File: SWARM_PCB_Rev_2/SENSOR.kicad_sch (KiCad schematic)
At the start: 14 parts

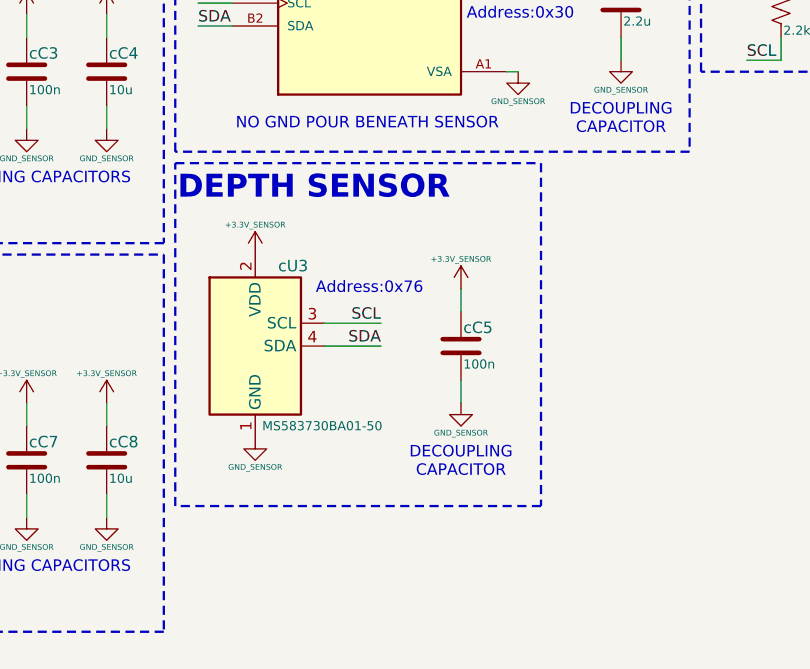
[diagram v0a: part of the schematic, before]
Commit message: Fixed some small errors and added the Output board
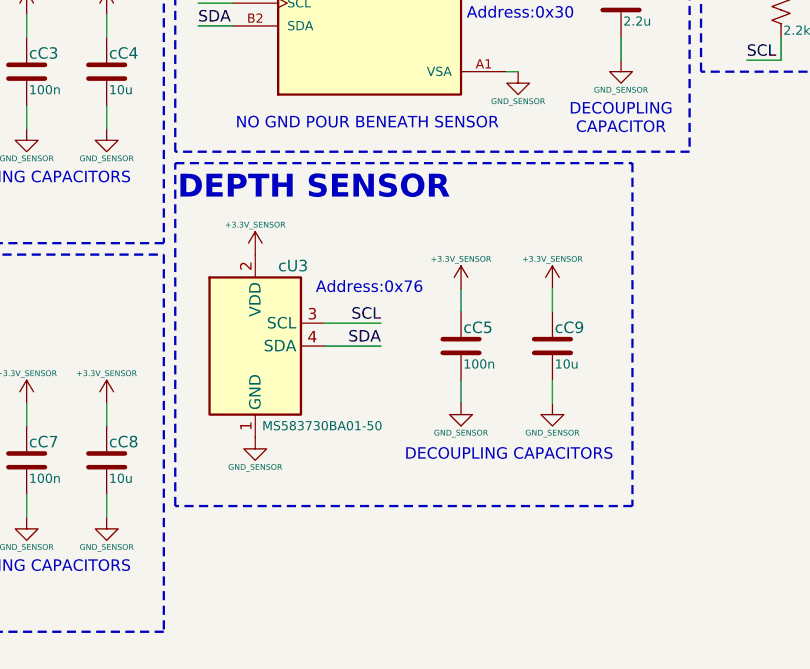
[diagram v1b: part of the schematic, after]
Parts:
- added cC9: 10u, Capacitor_SMD:C_0603_1608Metric, symbol Device:C
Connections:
- net +3.3V_SENSOR: now also cC9.2
- net GND_SENSOR: now also cC9.1
